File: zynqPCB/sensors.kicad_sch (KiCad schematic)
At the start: 22 parts, among them Q7 IRLML2502, SW1 TL6215RF200BDT, U13 VL53L1CXV0FY/1, U14 APDS-9960, U22 TSOP344, U23 LSM6DSLTR, U6 LIS2HH12

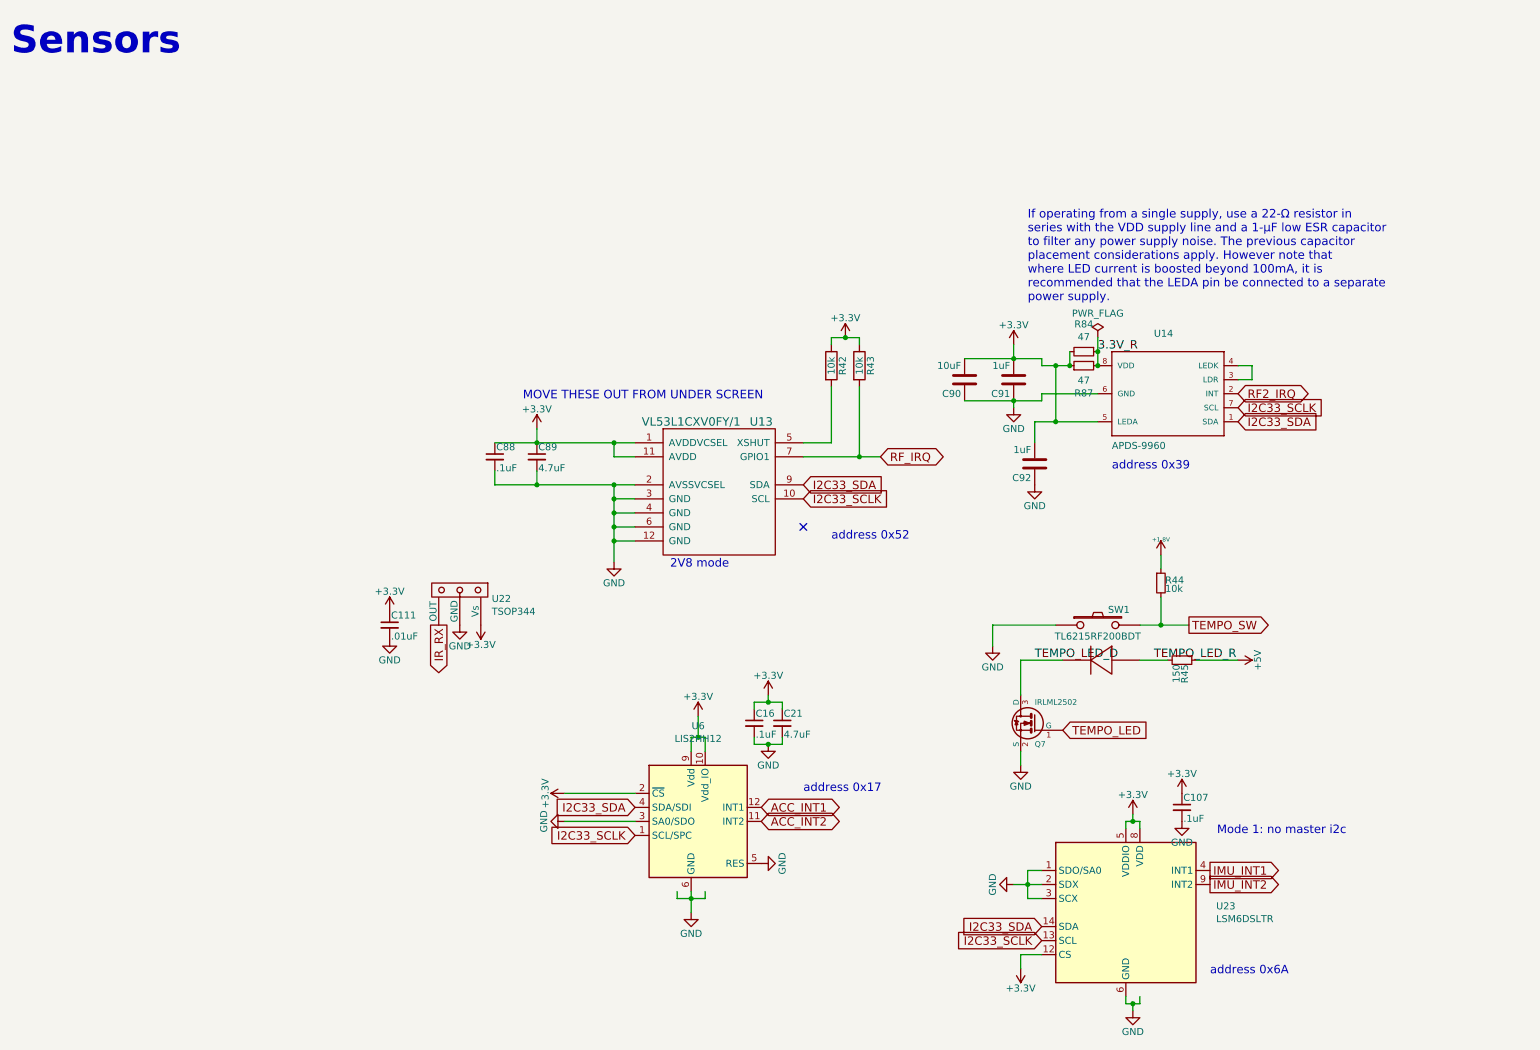
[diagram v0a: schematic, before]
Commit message: Remove Sensors
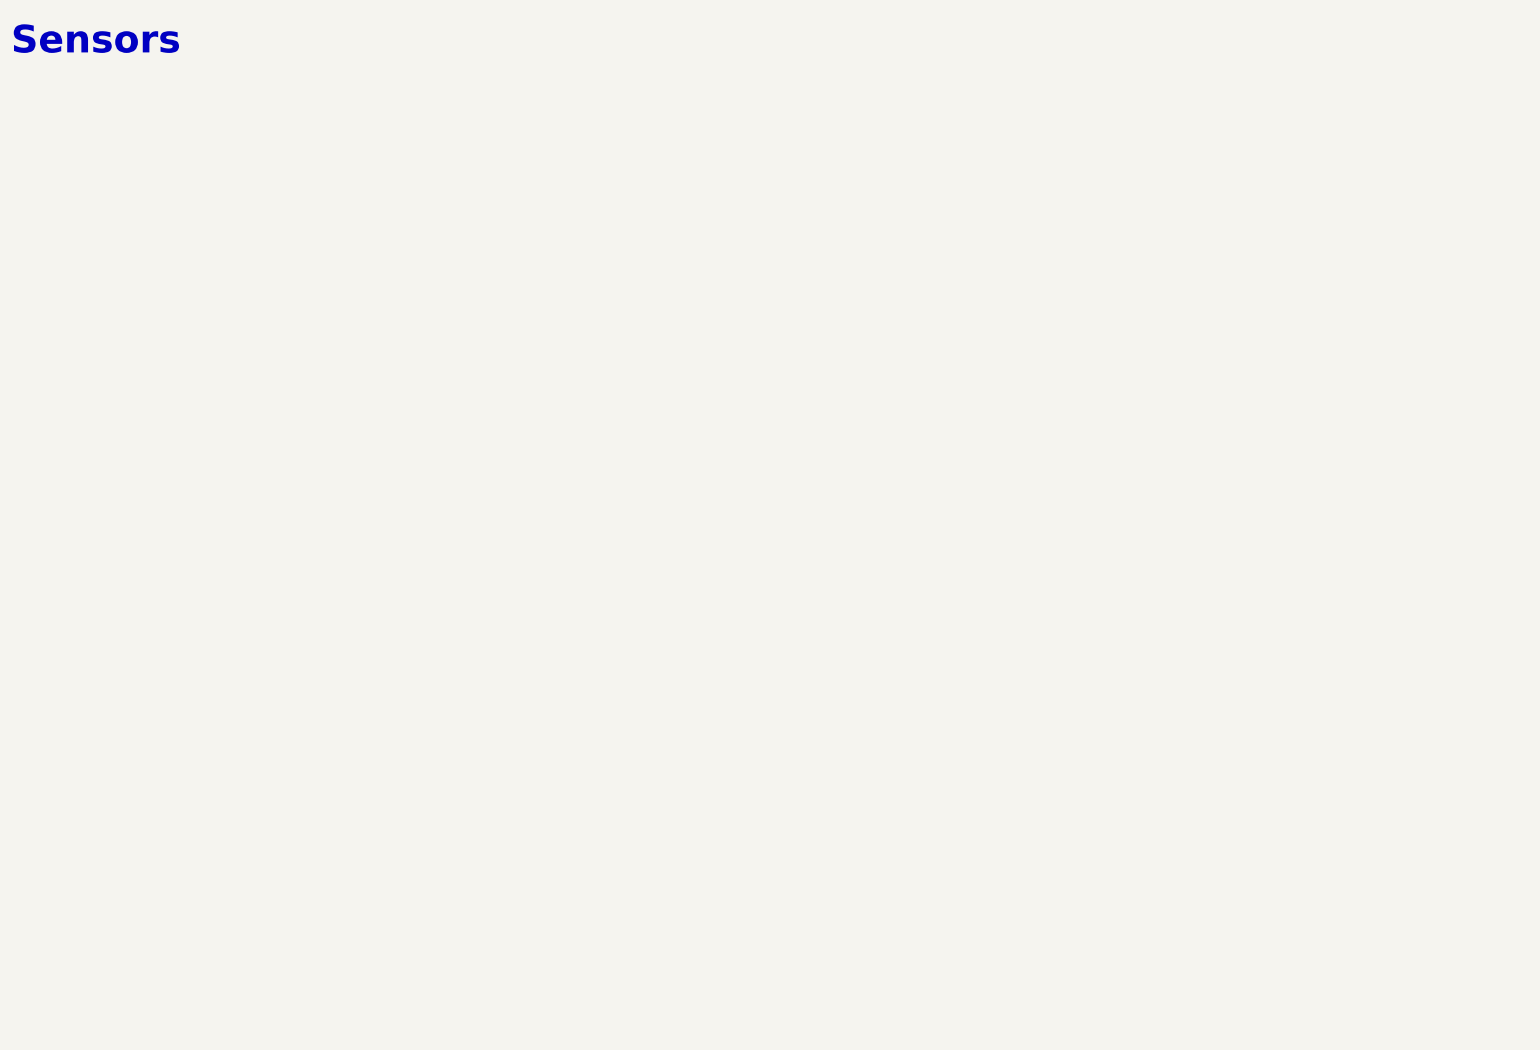
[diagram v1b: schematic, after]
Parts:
- removed C107, C16, C88: .1uF, Capacitor_SMD:C_0402_1005Metric, symbol Device:C_Small
- removed C111: .01uF, Capacitor_SMD:C_0402_1005Metric, symbol Device:C_Small
- removed C21, C89: 4.7uF, Capacitor_SMD:C_0402_1005Metric, symbol Device:C_Small
- removed C90: 10uF, Capacitor_SMD:C_0603_1608Metric, symbol Device:C
- removed C91, C92: 1uF, Capacitor_SMD:C_0402_1005Metric, symbol Device:C
- removed Q7: IRLML2502, Package_TO_SOT_SMD:SOT-23, symbol DFTBoard-rescue:IRLML2502-
- removed R42, R43: 10k, Resistor_SMD:R_0402_1005Metric, symbol Device:R
- removed R44: 10k, Resistor_SMD:R_0402_1005Metric, symbol Device:R_Small
- removed R45: 150, Resistor_SMD:R_0402_1005Metric, symbol Device:R_Small
- removed R84, R87: 47, Resistor_SMD:R_0402_1005Metric, symbol Device:R_Small
- removed SW1: TL6215RF200BDT, DFTcustom:tl6215_right_angle, symbol DFTBoard-rescue:SW_IL-
- removed U13: VL53L1CXV0FY/1, DFTcustom:Optical_LGA12, symbol DFTBoard-rescue:VL53L0X
- removed U14: APDS-9960, DFTcustom:APDS_9960, symbol DFTBoard-rescue:APDS-9960
- removed U22: TSOP344, DFTcustom:JUMPER_3PIN, symbol DFTCustom:TSOP344
- removed U23: LSM6DSLTR, Package_LGA:LGA-14_3x2.5mm_P0.5mm_LayoutBorder3x4y, symbol Sensor_Motion:LSM6DS3
- removed U6: LIS2HH12, Package_LGA:LGA-12_2x2mm_P0.5mm, symbol Sensor_Motion:LIS2HH12
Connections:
- no-connect marks 1 -> 0
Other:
- note removed: "2V8 mode"
- note removed: "If operating from a single supply, use a 22-Ω resistor in series with the VDD supply line and a 1-μF low ESR capacitor to filter any power supply noise. The previous capacitor placement considerations apply. However note that where LED current is boosted beyond 100mA, it is recommended that the LEDA pin be connected to a separate power supply."
- note removed: "MOVE THESE OUT FROM UNDER SCREEN"
- note removed: "Mode 1: no master i2c"
- note removed: "address 0x17"
- note removed: "address 0x39"
- note removed: "address 0x52"
- note removed: "address 0x6A"
